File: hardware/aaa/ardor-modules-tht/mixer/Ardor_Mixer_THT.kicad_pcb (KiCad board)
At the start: 2 copper layers, 100 x 75 mm, 30 parts, among them J101 5V POWER INPUT, J102 STEREO AUDIO INPUT FROM SOURCE, J103 BUFFERED STEREO + MONO AUDIO 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, U401 MCP6022-I/P, U402 MCP6022-I/P

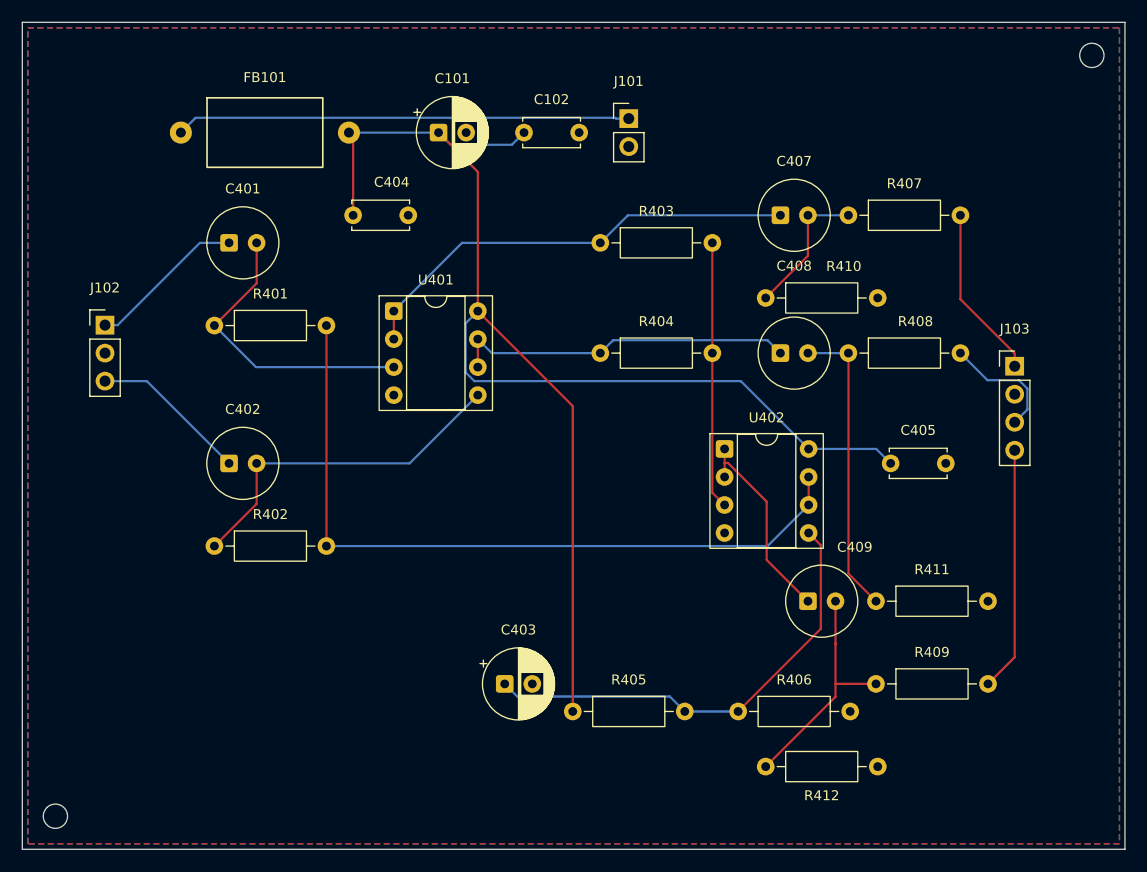
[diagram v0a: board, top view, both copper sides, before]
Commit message: feat(hardware): compact layouts and adopt Hestore module packages
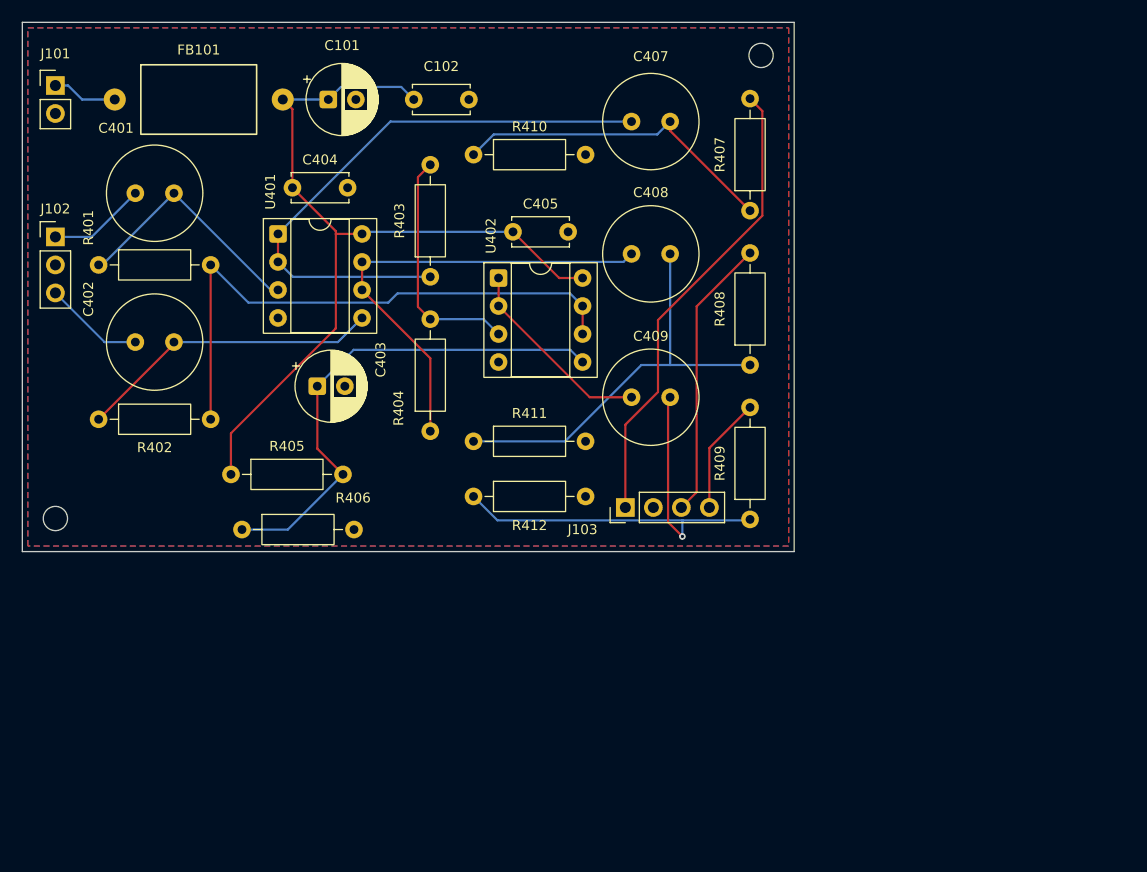
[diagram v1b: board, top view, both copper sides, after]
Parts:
- C401, C402, C407, C408, C409: value 10u / 25V BIPOLAR -> 10u / 50V BIPOLAR; footprint Ardor_THT:CP_Bipolar_D6.3mm_P2.50mm -> Ardor_THT:CP_Bipolar_Nichicon_D8.0mm_P3.50mm
- moved J101 52.1 mm to (53.0, 55.7)
- moved R406 47.9 mm to (69.9, 96.0)
- moved C405 40.2 mm to (94.5, 69.0)
- moved R411 39.3 mm to (90.9, 88.0)
- moved R405 37.7 mm to (68.9, 91.0)
- moved J103 37.6 mm to (104.7, 94.0), turned to 90 degrees
- moved R412 36.1 mm to (90.9, 93.0)
- moved C403 31.9 mm to (76.8, 83.0)
- moved H2 30.0 mm to (117.0, 53.0)
- moved R410 29.5 mm to (90.9, 62.0)
- moved H1 27.0 mm to (53.0, 95.0)
- moved U402 25.7 mm to (93.2, 73.2)
- moved C409 24.5 mm to (105.2, 84.0)
- moved R409 18.8 mm to (116.0, 95.1), turned to 90 degrees
- moved R404 17.0 mm to (87.0, 87.1), turned to 90 degrees
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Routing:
- net /+5V_A: track 130.0 -> 76.9 mm
- net /+5V: track 41.2 -> 5.91 mm
- net Net-(J103-Pin_1): track 15.7 -> 42.7 mm
- net Net-(C409-Pad2): track 21.3 -> 40.7 mm, vias 0 -> 1
- net Net-(C407-Pad2): track 12.8 -> 30.2 mm
- net /VREF: track 67.8 -> 52.5 mm
- net Net-(J103-Pin_3): track 10.9 -> 25.7 mm
- net Net-(U401A--): track 41.2 -> 53.2 mm
- net Net-(J103-Pin_4): track 22.2 -> 10.6 mm
- net Net-(U401B--): track 31.5 -> 42.7 mm
- net Net-(C408-Pad2): track 27.2 -> 38.0 mm
- net Net-(J102-Pin_1): track 14.3 -> 8.89 mm
- net Net-(J102-Pin_3): track 14.3 -> 9.10 mm
- net Net-(U401A-+): track 26.9 -> 22.7 mm
- net Net-(U402B-+): track 42.0 -> 46.1 mm
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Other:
- board size 100 x 75 mm -> 70 x 48 mm
